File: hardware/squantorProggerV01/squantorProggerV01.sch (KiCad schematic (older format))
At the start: 8 parts, among them J1 USB-ID, J2 JTAG_2X05_IN, J3 JTAG_2X05_OUT

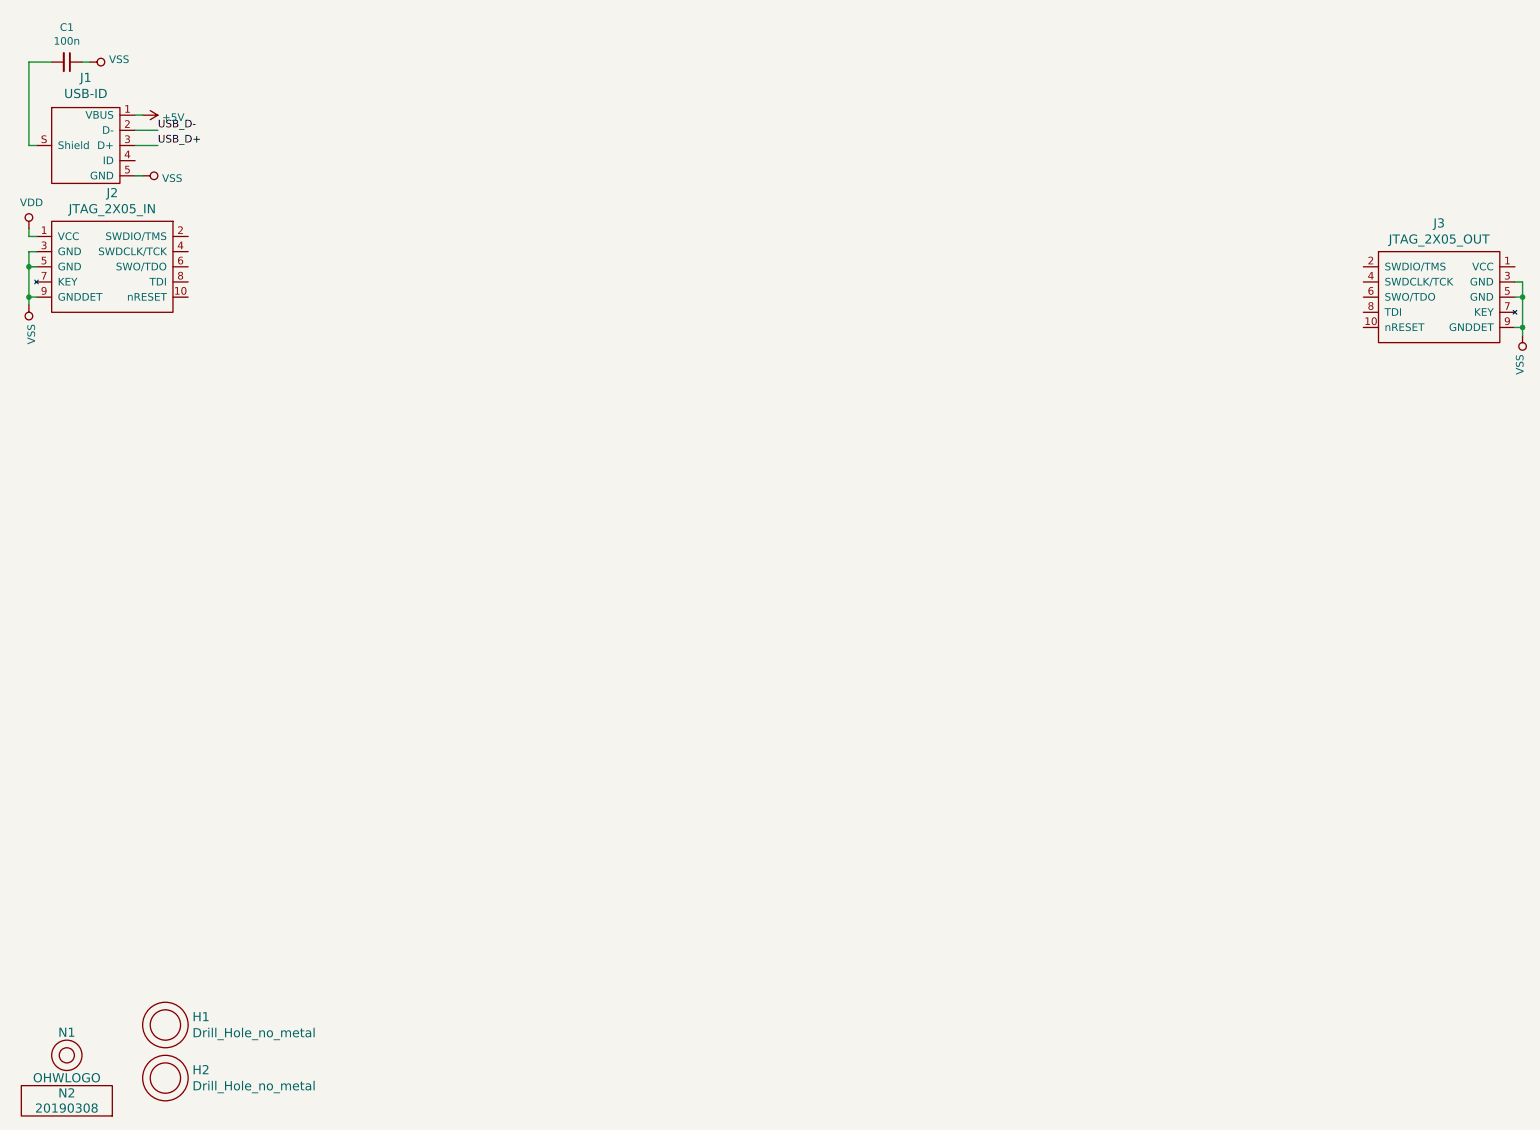
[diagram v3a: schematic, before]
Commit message: imported schematics of LPC824 breakout and HT42B534 breakout
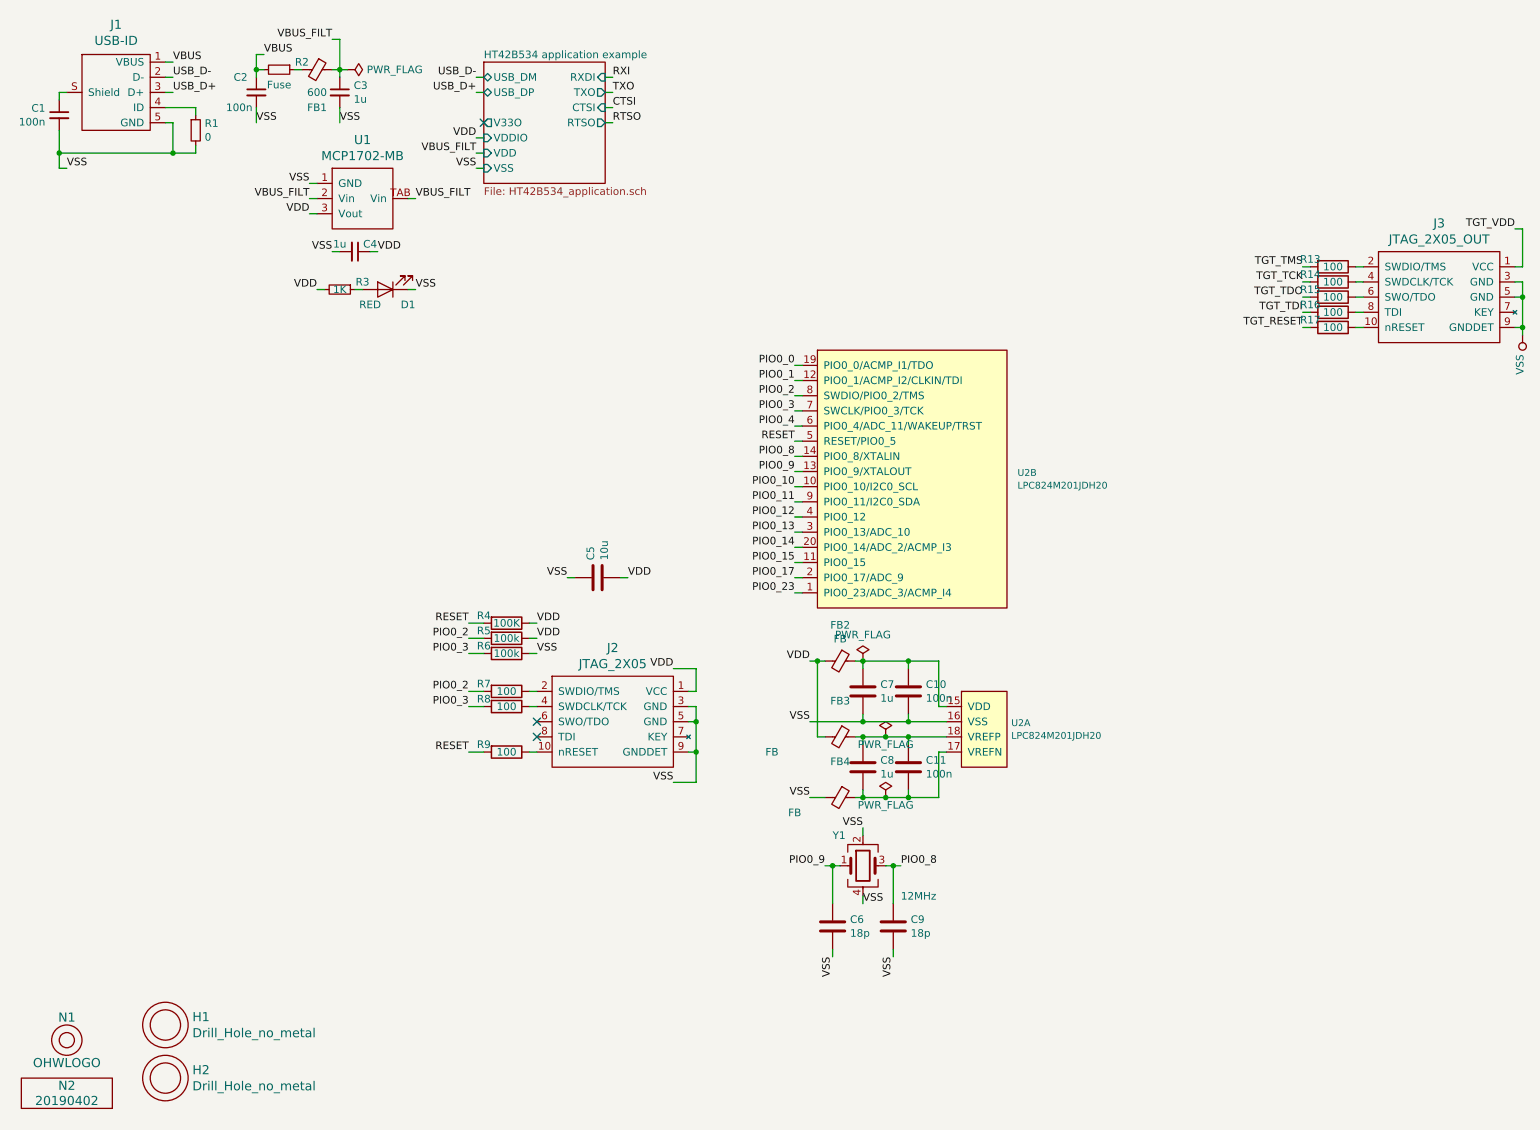
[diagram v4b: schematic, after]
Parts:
- removed J1: USB-ID, SquantorUsb:USB-muB-SMD_TH, symbol squantorProggerV01-rescue:USB-ID-SquantorUsb
- removed J2: JTAG_2X05_IN, SquantorConnectors:Header-0127-2X05-H006, symbol SquantorConnectors:JTAG_2X05_IN
- added C10, C11: 100n, SquantorRcl:C_0402, symbol Device:C
- added C2: 100n, SquantorRcl:C_0603, symbol Device:C_Small
- added C3, C4: 1u, SquantorRcl:C_0603, symbol Device:C_Small
- added C5: 10u, SquantorRcl:C_0805, symbol Device:C
- added C6, C9: 18p, SquantorRcl:C_0402, symbol Device:C
- added C7, C8: 1u, SquantorRcl:C_0603, symbol Device:C
- added D1: RED, SquantorDiodes:D_0603_hand, symbol Device:LED
- added FB1: 600, SquantorRcl:R_0603_hand, symbol Device:Ferrite_Bead_Small
- added FB2, FB3, FB4: FB, SquantorRcl:C_0402, symbol Device:Ferrite_Bead_Small
- added J1: USB-ID, SquantorUsb:USB-muB-SMD_TH, symbol SquantorUsb:USB-ID
- added J2: JTAG_2X05, SquantorConnectors:Header-0127-2X05-H006, symbol SquantorConnectors:JTAG_2X05
- added R1: 0, SquantorRcl:R_0402_hand, symbol Device:R_Small
- added R13, R14, R15, R16, R17, R7, R8, R9: 100, SquantorRcl:R_0402_hand, symbol Device:R
- added R2: Fuse, SquantorRcl:R_0603_hand, symbol Device:R_Small
- added R3: 1K, SquantorRcl:R_0402_hand, symbol Device:R_Small
- added R4: 100K, SquantorRcl:R_0402_hand, symbol Device:R
- added R5, R6: 100k, SquantorRcl:R_0402_hand, symbol Device:R
- added U1: MCP1702-MB, SquantorIC:SOT89-ViaTab-Microchip-MB, symbol SquantorMicrochip:MCP1702-MB
- added U2: LPC824M201JDH20, SquantorIC:SOT360, symbol SquantorNxp:LPC824M201JDH20
- added Y1: 12MHz, SquantorCrystal:Crystal_3225_4, symbol Device:Crystal_GND24
- N1: footprint Symbols:OSHW-Symbol_6.7x6mm_SilkScreen -> Symbol:OSHW-Symbol_6.7x6mm_SilkScreen
- N2: value 20190308 -> 20190402
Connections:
- net USB_D+: now also J1.3 (D+)
- net USB_D-: now also J1.2 (D-)
- net VDD: now also C4.1, C5.2, FB2.2, FB3.2, J2.1 (VCC), R3.2, R4.1, R5.1, U1.3 (Vout)
- net VSS: now also C1.2, C10.2, C2.2, C3.2, C4.2, C5.1, C6.2, C7.2, C9.2, D1.1 (K), FB4.2, J1.5 (GND), J2.3 (GND), J2.5 (GND), J2.9 (GNDDET), R1.2, R6.1, U1.1 (GND), U2.16 (VSS), Y1.2, Y1.4; no longer C1.1
- net TGT_VDD: now reaches J3.1 (VCC)
- net at J3.10 (nRESET): now also R17.1
- net at J3.2 (SWDIO/TMS): now also R13.1
- net at J3.4 (SWDCLK/TCK): now also R14.1
- net at J3.6 (SWO/TDO): now also R15.1
- net at J3.8 (TDI): now also R16.1
- new net: C11.1, C8.1, FB3.1, U2.18 (VREFP)
- new net: C11.2, C8.2, FB4.1, U2.17 (VREFN)
- new net: C10.1, C7.1, FB2.1, U2.15 (VDD)
- new net: J2.10 (nRESET), R9.1
- new net: J2.2 (SWDIO/TMS), R7.1
- new net: J2.4 (SWDCLK/TCK), R8.1
- new net: J1.4 (ID), R1.1
- new net: C1.1, J1.S (Shield)
- new net: FB1.2, R2.1
- new net: D1.2 (A), R3.1
- new net PIO0_0: U2.19 (PIO0_0/ACMP_I1/TDO)
- new net PIO0_1: U2.12 (PIO0_1/ACMP_I2/CLKIN/TDI)
- new net PIO0_10: U2.10 (PIO0_10/I2C0_SCL)
- new net PIO0_11: U2.9 (PIO0_11/I2C0_SDA)
- new net PIO0_12: U2.4 (PIO0_12)
- new net PIO0_13: U2.3 (PIO0_13/ADC_10)
- new net PIO0_14: U2.20 (PIO0_14/ADC_2/ACMP_I3)
- new net PIO0_15: U2.11 (PIO0_15)
- new net PIO0_17: U2.2 (PIO0_17/ADC_9)
- new net PIO0_2: R5.2, R7.2, U2.8 (SWDIO/PIO0_2/TMS)
- new net PIO0_23: U2.1 (PIO0_23/ADC_3/ACMP_I4)
- new net PIO0_3: R6.2, R8.2, U2.7 (SWCLK/PIO0_3/TCK)
- new net PIO0_4: U2.6 (PIO0_4/ADC_11/WAKEUP/TRST)
- new net PIO0_8: C9.1, U2.14 (PIO0_8/XTALIN), Y1.3
- new net PIO0_9: C6.1, U2.13 (PIO0_9/XTALOUT), Y1.1
- new net RESET: R4.2, R9.2, U2.5 (RESET/PIO0_5)
- new net TGT_RESET: R17.2
- new net TGT_TCK: R14.2
- new net TGT_TDI: R16.2
- new net TGT_TDO: R15.2
- new net TGT_TMS: R13.2
- new net VBUS: C2.1, J1.1 (VBUS), R2.2
- new net VBUS_FILT: C3.1, FB1.1, U1.2 (Vin), U1.TAB (Vin)
- no-connect marks 0 -> 3

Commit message: added test points to USB and SWD in
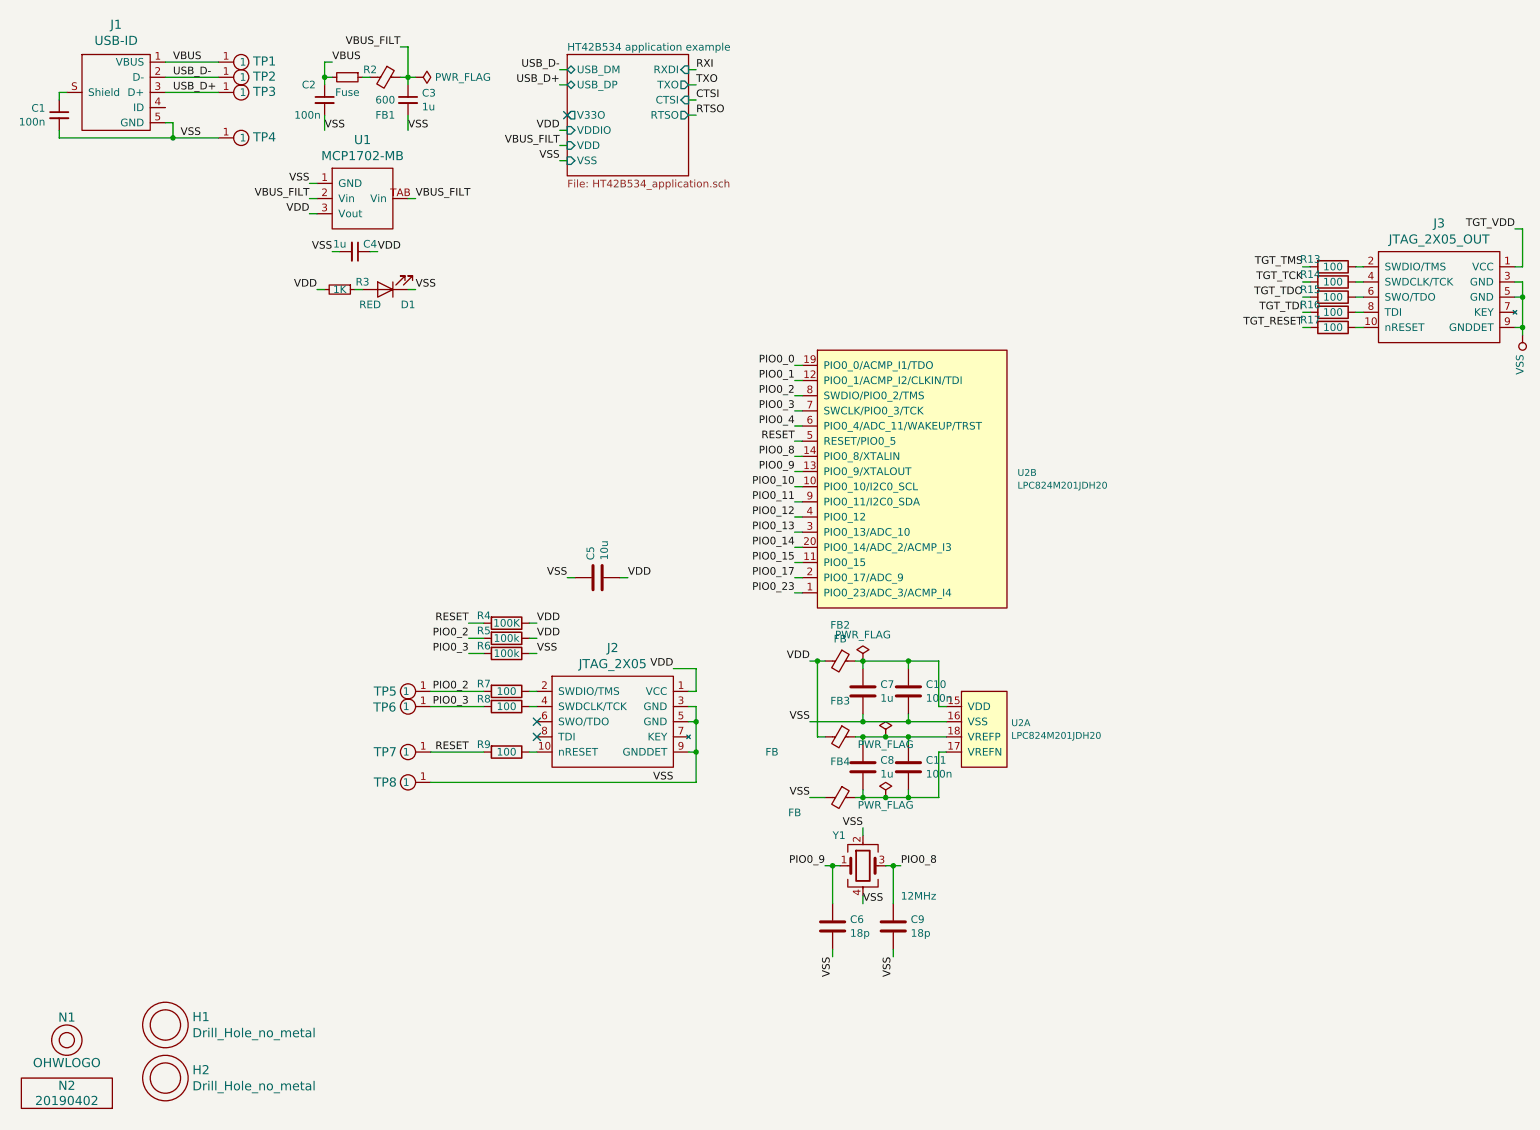
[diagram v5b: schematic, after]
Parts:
- removed R1: 0, SquantorRcl:R_0402_hand, symbol Device:R_Small
- added TP1, TP2, TP3, TP4, TP5, TP6, TP7, TP8: testpad, SquantorTestPoints:TestPoint_Hole_D0.8mm, symbol SquantorProto:testpad
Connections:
- net PIO0_2: now also TP5.1
- net PIO0_3: now also TP6.1
- net RESET: now also TP7.1
- net USB_D+: now also TP3.1
- net USB_D-: now also TP2.1
- net VBUS: now also TP1.1
- net VSS: now also TP4.1, TP8.1
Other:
- moved on the sheet: C2, C3, FB1, R2

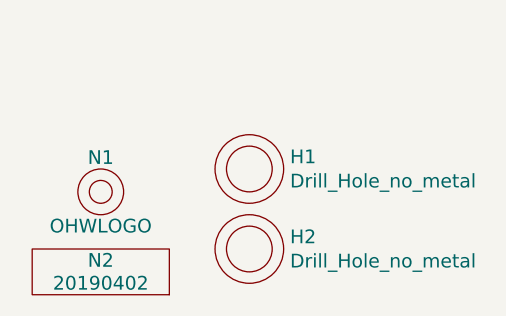
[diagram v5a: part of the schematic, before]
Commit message: updated footprint
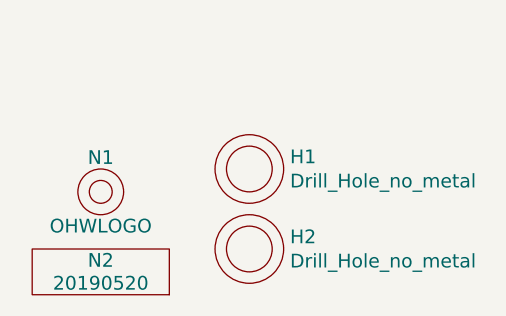
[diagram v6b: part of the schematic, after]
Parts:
- N2: value 20190402 -> 20190520
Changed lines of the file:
@@
 P 850 7650
 F 0 "N2" H 850 7750 60  0000 C CNN
-F 1 "20190402" H 850 7650 60  0000 C CNN
+F 1 "20190520" H 850 7650 60  0000 C CNN
 F 2 "SquantorLabels:Label_version" H 850 7650 60  0001 C CNN
 F 3 "" H 850 7650 60  0001 C CNN
